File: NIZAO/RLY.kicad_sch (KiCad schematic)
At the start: 3 parts, among them K1 G5V-1, K2 G5V-1, U18 LK1802

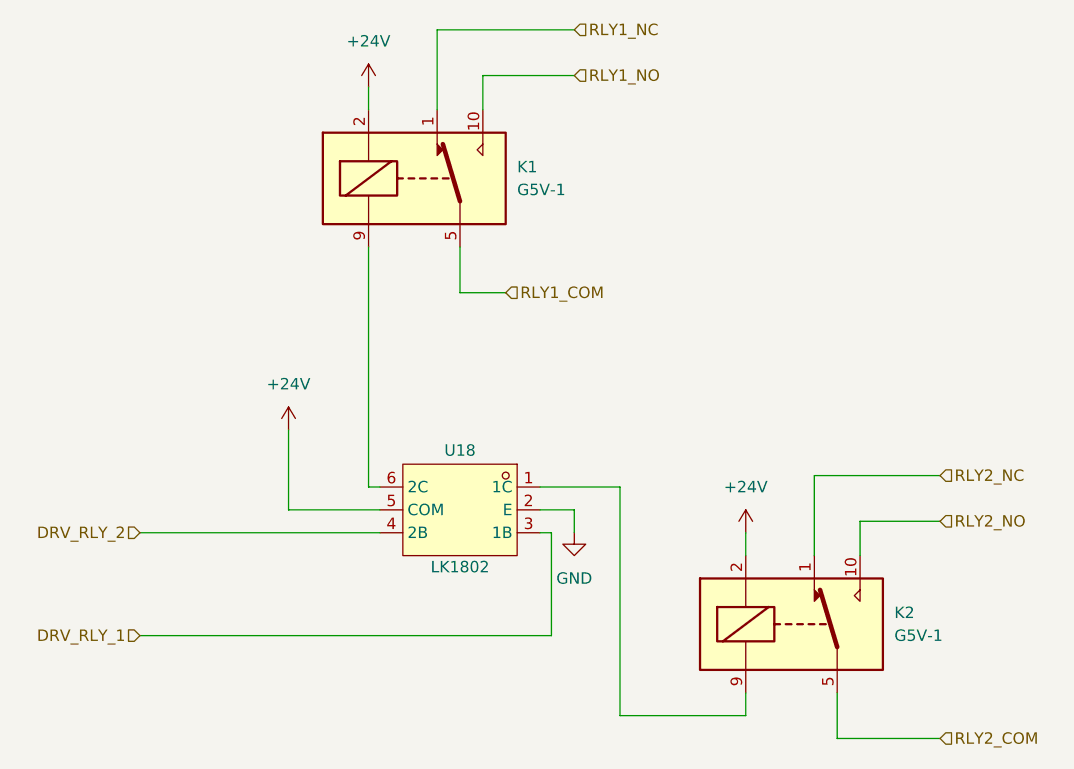
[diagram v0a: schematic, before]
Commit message: Colocandos los 3d de los componetes en la placa NIZAO
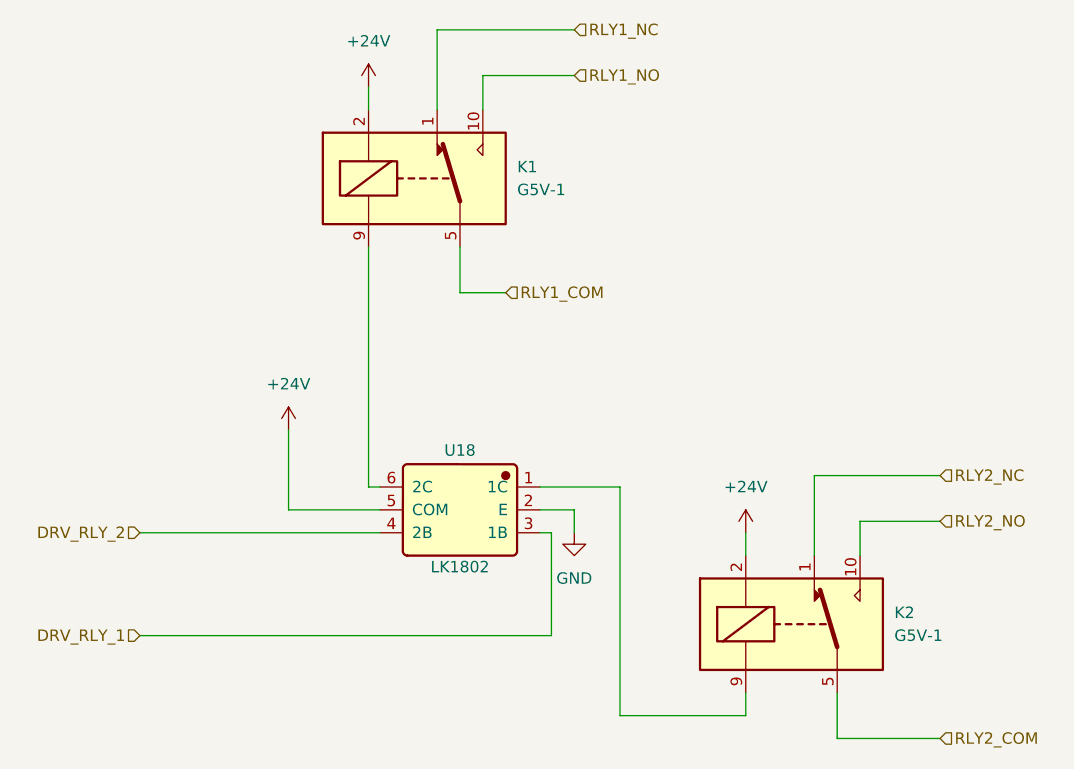
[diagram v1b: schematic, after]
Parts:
- U18: footprint LANKE LK1802:SOT-23-6_L2.9-W1.6-P0.95-LS2.8-BR -> JLCImport:LK1802; symbol easyeda2kicad:LK1802 -> JLCImport:LK1802; LCSC (none) -> C2984831; Manufacturer (none) -> LANKE; Manufacturer Part (none) -> LK1802
